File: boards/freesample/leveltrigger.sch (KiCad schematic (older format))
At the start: 0 parts

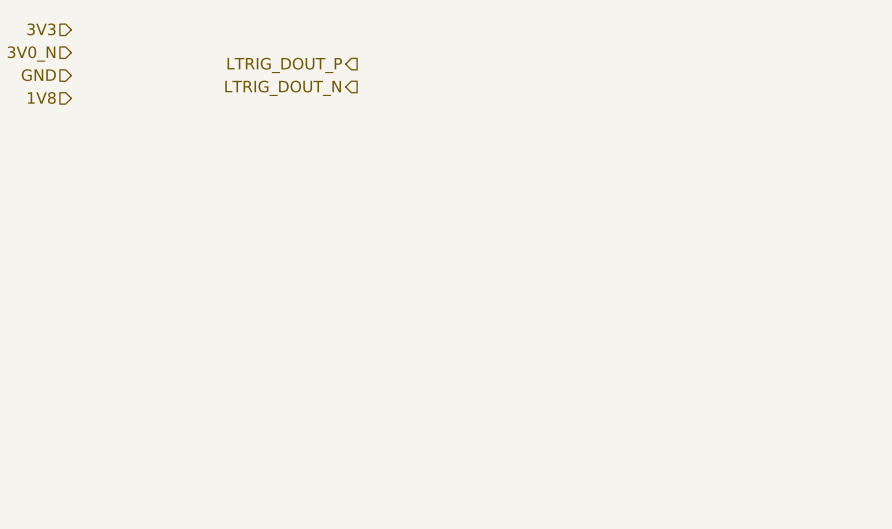
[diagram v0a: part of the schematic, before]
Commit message: Continued initial schematic capture
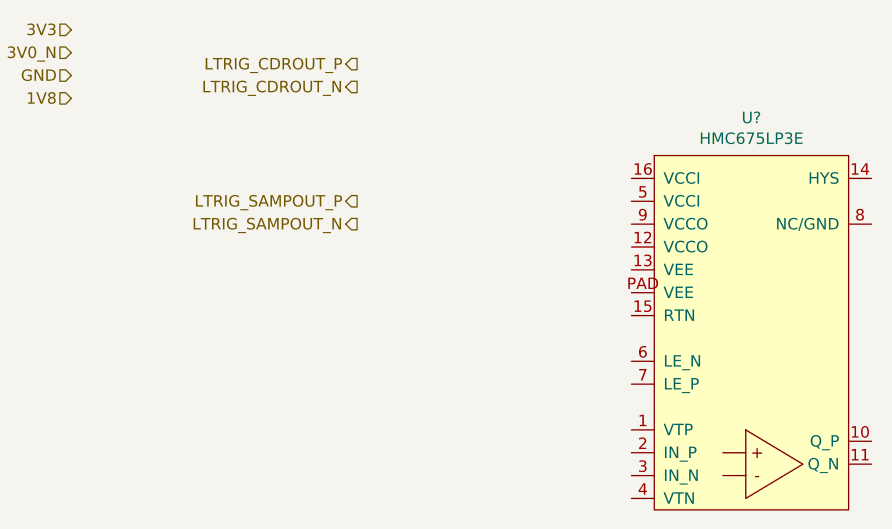
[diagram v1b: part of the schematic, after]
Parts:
- added U?: HMC675LP3E, symbol analog-azonenberg:HMC675LP3E
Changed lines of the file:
@@
 $Descr A4 11693 8268
 encoding utf-8
-Sheet 9 11
+Sheet 8 12
 Title "FREESAMPLE Oscilloscope"
-Date "2018-12-15"
+Date "2018-12-17"
 Rev "0.1"
 Comp "Andrew D. Zonenberg / Antikernel Labs"
@@
 LTRIG_DIN
 Text HLabel 5550 1650 0    50   Output ~ 0
-LTRIG_DOUT_P
+LTRIG_CDROUT_P
 Text HLabel 5550 1750 0    50   Output ~ 0
-LTRIG_DOUT_N
+LTRIG_CDROUT_N
 Text HLabel 4300 1500 0    50   Input ~ 0
 3V3
@@
 Text HLabel 3400 2100 0    50   Input ~ 0
 LTRIG_VT
+Text HLabel 5550 2250 0    50   Output ~ 0
+LTRIG_SAMPOUT_P
+Text HLabel 5550 2350 0    50   Output ~ 0
+LTRIG_SAMPOUT_N
+$Comp
+L analog-azonenberg:HMC675LP3E U?
+U 1 1 5C3D1034
+P 6850 3600
+F 0 "U?" H 7275 5315 50  0000 C CNN
+F 1 "HMC675LP3E" H 7275 5224 50  0000 C CNN
+F 2 "" H 6850 3600 50  0001 C CNN
+F 3 "" H 6850 3600 50  0001 C CNN
+	1    6850 3600
+	1    0    0    -1
+$EndComp
 $EndSCHEMATC

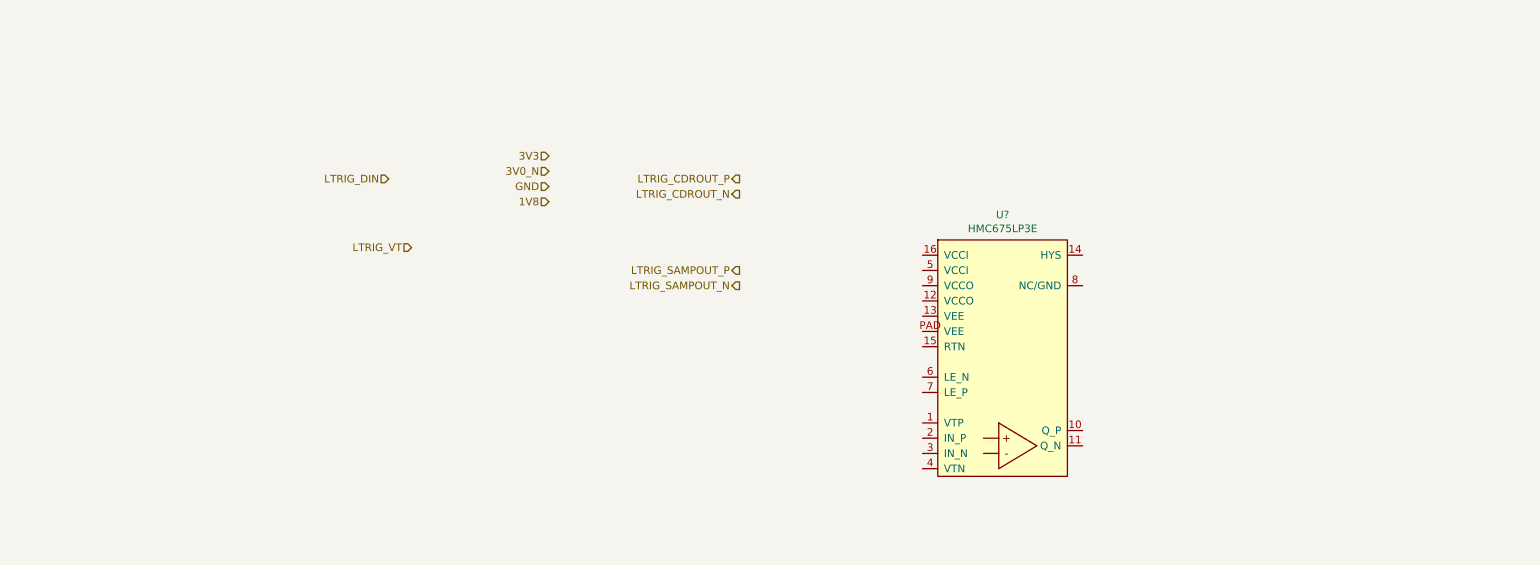
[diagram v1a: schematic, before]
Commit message: Continued initial schematic entry
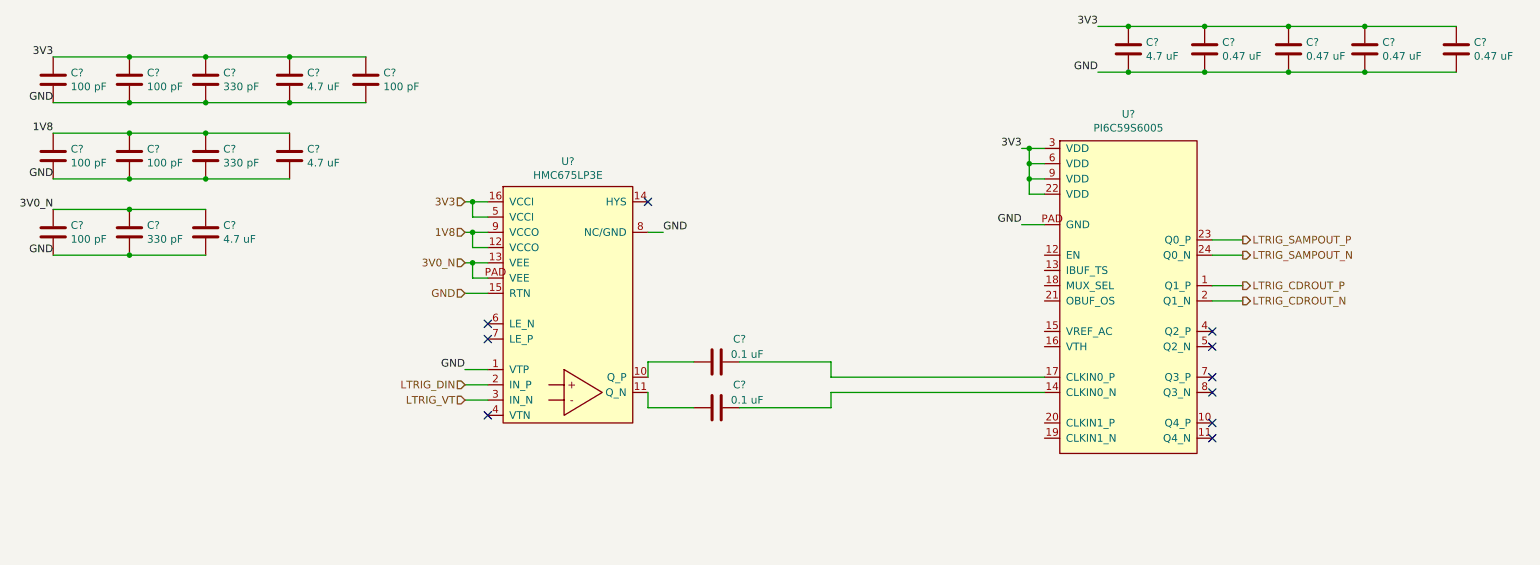
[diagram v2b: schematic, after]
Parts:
- added C? (x3): 330 pF, symbol device:C
- added C? (x6): 100 pF, symbol device:C
- added C? (x4): 4.7 uF, symbol device:C
- added C? (x4): 0.47 uF, symbol device:C
- added C? (x2): 0.1 uF, symbol device:C
- added U?: PI6C59S6005, symbol special-azonenberg:PI6C59S6005
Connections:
- net 1V8: now also U?.12 (VCCO), U?.9 (VCCO), C?.1, C?.1, C?.1, C?.1
- net 3V0_N: now also U?.13 (VEE), U?.PAD (VEE), C?.1, C?.1, C?.1
- net 3V3: now also U?.16 (VCCI), U?.5 (VCCI), C?.1, C?.1, C?.1, C?.1, C?.1, C?.1, C?.1, C?.1, C?.1, C?.1, U?.22 (VDD), U?.3 (VDD), U?.6 (VDD), U?.9 (VDD)
- net GND: now also U?.1 (VTP), U?.15 (RTN), U?.8 (NC/GND), C?.2, C?.2, C?.2, C?.2, C?.2, C?.2, C?.2, C?.2, C?.2, C?.2, C?.2, C?.2, C?.2, C?.2, C?.2, C?.2, C?.2, U?.PAD (GND)
- net LTRIG_CDROUT_N: now also U?.2 (Q1_N)
- net LTRIG_CDROUT_P: now also U?.1 (Q1_P)
- net LTRIG_DIN: now also U?.2 (IN_P)
- net LTRIG_SAMPOUT_N: now also U?.24 (Q0_N)
- net LTRIG_SAMPOUT_P: now also U?.23 (Q0_P)
- net LTRIG_VT: now also U?.3 (IN_N)
- net at U?.10 (Q_P): now also C?.2
- net at U?.11 (Q_N): now also C?.2
- new net: C?.1, U?.14 (CLKIN0_N)
- new net: C?.1, U?.17 (CLKIN0_P)
- no-connect marks 0 -> 10
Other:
- moved on the sheet: U?

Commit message: Continued work on schematic capture
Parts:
- gave numbers to parts that had none: 21
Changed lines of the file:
@@
 LTRIG_SAMPOUT_N
 $Comp
-L analog-azonenberg:HMC675LP3E U?
+L analog-azonenberg:HMC675LP3E U9
 U 1 1 5C3D1034
 P 4000 3250
-F 0 "U?" H 4425 4965 50  0000 C CNN
+F 0 "U9" H 4425 4965 50  0000 C CNN
 F 1 "HMC675LP3E" H 4425 4874 50  0000 C CNN
 F 2 "" H 4000 3250 50  0001 C CNN
@@
 P 2050 1000
 AR Path="/5C0E404A/5C5773C7" Ref="C?"  Part="1"
-AR Path="/5C23AE1C/5C5773C7" Ref="C?"  Part="1"
-F 0 "C?" H 2165 1046 50  0000 L CNN
+AR Path="/5C23AE1C/5C5773C7" Ref="C43"  Part="1"
+F 0 "C43" H 2165 1046 50  0000 L CNN
 F 1 "330 pF" H 2165 955 50  0000 L CNN
 F 2 "" H 2088 850 50  0001 C CNN
@@
 P 1550 1000
 AR Path="/5C0E404A/5C5773CD" Ref="C?"  Part="1"
-AR Path="/5C23AE1C/5C5773CD" Ref="C?"  Part="1"
-F 0 "C?" H 1665 1046 50  0000 L CNN
+AR Path="/5C23AE1C/5C5773CD" Ref="C40"  Part="1"
+F 0 "C40" H 1665 1046 50  0000 L CNN
 F 1 "100 pF" H 1665 955 50  0000 L CNN
 F 2 "" H 1588 850 50  0001 C CNN
@@
 P 1050 1000
 AR Path="/5C0E404A/5C5773D3" Ref="C?"  Part="1"
-AR Path="/5C23AE1C/5C5773D3" Ref="C?"  Part="1"
-F 0 "C?" H 1165 1046 50  0000 L CNN
+AR Path="/5C23AE1C/5C5773D3" Ref="C37"  Part="1"
+F 0 "C37" H 1165 1046 50  0000 L CNN
 F 1 "100 pF" H 1165 955 50  0000 L CNN
 F 2 "" H 1088 850 50  0001 C CNN
@@
 P 2600 1000
 AR Path="/5C0E404A/5C5773DB" Ref="C?"  Part="1"
-AR Path="/5C23AE1C/5C5773DB" Ref="C?"  Part="1"
-F 0 "C?" H 2715 1046 50  0000 L CNN
+AR Path="/5C23AE1C/5C5773DB" Ref="C46"  Part="1"
+F 0 "C46" H 2715 1046 50  0000 L CNN
 F 1 "4.7 uF" H 2715 955 50  0000 L CNN
 F 2 "" H 2638 850 50  0001 C CNN
@@
 P 3100 1000
 AR Path="/5C0E404A/5C5773EB" Ref="C?"  Part="1"
-AR Path="/5C23AE1C/5C5773EB" Ref="C?"  Part="1"
-F 0 "C?" H 3215 1046 50  0000 L CNN
+AR Path="/5C23AE1C/5C5773EB" Ref="C48"  Part="1"
+F 0 "C48" H 3215 1046 50  0000 L CNN
 F 1 "100 pF" H 3215 955 50  0000 L CNN
 F 2 "" H 3138 850 50  0001 C CNN
@@
 P 2050 1500
 AR Path="/5C0E404A/5C5773F5" Ref="C?"  Part="1"
-AR Path="/5C23AE1C/5C5773F5" Ref="C?"  Part="1"
-F 0 "C?" H 2165 1546 50  0000 L CNN
+AR Path="/5C23AE1C/5C5773F5" Ref="C44"  Part="1"
+F 0 "C44" H 2165 1546 50  0000 L CNN
 F 1 "330 pF" H 2165 1455 50  0000 L CNN
 F 2 "" H 2088 1350 50  0001 C CNN
@@
 P 1550 1500
 AR Path="/5C0E404A/5C5773FB" Ref="C?"  Part="1"
-AR Path="/5C23AE1C/5C5773FB" Ref="C?"  Part="1"
-F 0 "C?" H 1665 1546 50  0000 L CNN
+AR Path="/5C23AE1C/5C5773FB" Ref="C41"  Part="1"
+F 0 "C41" H 1665 1546 50  0000 L CNN
 F 1 "100 pF" H 1665 1455 50  0000 L CNN
 F 2 "" H 1588 1350 50  0001 C CNN
@@
 P 1050 1500
 AR Path="/5C0E404A/5C577401" Ref="C?"  Part="1"
-AR Path="/5C23AE1C/5C577401" Ref="C?"  Part="1"
-F 0 "C?" H 1165 1546 50  0000 L CNN
+AR Path="/5C23AE1C/5C577401" Ref="C38"  Part="1"
+F 0 "C38" H 1165 1546 50  0000 L CNN
 F 1 "100 pF" H 1165 1455 50  0000 L CNN
 F 2 "" H 1088 1350 50  0001 C CNN
@@
 P 2600 1500
 AR Path="/5C0E404A/5C577409" Ref="C?"  Part="1"
-AR Path="/5C23AE1C/5C577409" Ref="C?"  Part="1"
-F 0 "C?" H 2715 1546 50  0000 L CNN
+AR Path="/5C23AE1C/5C577409" Ref="C47"  Part="1"
+F 0 "C47" H 2715 1546 50  0000 L CNN
 F 1 "4.7 uF" H 2715 1455 50  0000 L CNN
 F 2 "" H 2638 1350 50  0001 C CNN
@@
 P 1050 2000
 AR Path="/5C0E404A/5C57741A" Ref="C?"  Part="1"
-AR Path="/5C23AE1C/5C57741A" Ref="C?"  Part="1"
-F 0 "C?" H 1165 2046 50  0000 L CNN
+AR Path="/5C23AE1C/5C57741A" Ref="C39"  Part="1"
+F 0 "C39" H 1165 2046 50  0000 L CNN
 F 1 "100 pF" H 1165 1955 50  0000 L CNN
 F 2 "" H 1088 1850 50  0001 C CNN
@@
 P 1550 2000
 AR Path="/5C0E404A/5C577420" Ref="C?"  Part="1"
-AR Path="/5C23AE1C/5C577420" Ref="C?"  Part="1"
-F 0 "C?" H 1665 2046 50  0000 L CNN
+AR Path="/5C23AE1C/5C577420" Ref="C42"  Part="1"
+F 0 "C42" H 1665 2046 50  0000 L CNN
 F 1 "330 pF" H 1665 1955 50  0000 L CNN
 F 2 "" H 1588 1850 50  0001 C CNN
@@
 P 2050 2000
 AR Path="/5C0E404A/5C577426" Ref="C?"  Part="1"
-AR Path="/5C23AE1C/5C577426" Ref="C?"  Part="1"
-F 0 "C?" H 2165 2046 50  0000 L CNN
+AR Path="/5C23AE1C/5C577426" Ref="C45"  Part="1"
+F 0 "C45" H 2165 2046 50  0000 L CNN
 F 1 "4.7 uF" H 2165 1955 50  0000 L CNN
 F 2 "" H 2088 1850 50  0001 C CNN
@@
 P 7650 3450
 AR Path="/5C0E404A/5C5902BE" Ref="U?"  Part="1"
-AR Path="/5C23AE1C/5C5902BE" Ref="U?"  Part="1"
-F 0 "U?" H 8100 5675 50  0000 C CNN
+AR Path="/5C23AE1C/5C5902BE" Ref="U10"  Part="1"
+F 0 "U10" H 8100 5675 50  0000 C CNN
 F 1 "PI6C59S6005" H 8100 5584 50  0000 C CNN
 F 2 "" H 7650 3150 50  0001 C CNN
@@
 $EndComp
 $Comp
-L device:C C?
+L device:C C51
 U 1 1 5C5902C4
 P 8100 800
-F 0 "C?" H 8215 846 50  0000 L CNN
+F 0 "C51" H 8215 846 50  0000 L CNN
 F 1 "4.7 uF" H 8215 755 50  0000 L CNN
 F 2 "" H 8138 650 50  0001 C CNN
@@
 $EndComp
 $Comp
-L device:C C?
+L device:C C52
 U 1 1 5C5902CA
 P 8600 800
-F 0 "C?" H 8715 846 50  0000 L CNN
+F 0 "C52" H 8715 846 50  0000 L CNN
 F 1 "0.47 uF" H 8715 755 50  0000 L CNN
 F 2 "" H 8638 650 50  0001 C CNN
@@
 $EndComp
 $Comp
-L device:C C?
+L device:C C54
 U 1 1 5C5902D0
 P 9650 800
-F 0 "C?" H 9765 846 50  0000 L CNN
+F 0 "C54" H 9765 846 50  0000 L CNN
 F 1 "0.47 uF" H 9765 755 50  0000 L CNN
 F 2 "" H 9688 650 50  0001 C CNN
@@
 	8600 950  9150 950
 $Comp
-L device:C C?
+L device:C C53
 U 1 1 5C5902E2
 P 9150 800
-F 0 "C?" H 9265 846 50  0000 L CNN
+F 0 "C53" H 9265 846 50  0000 L CNN
 F 1 "0.47 uF" H 9265 755 50  0000 L CNN
 F 2 "" H 9188 650 50  0001 C CNN
@@
 	9150 950  9650 950
 $Comp
-L device:C C?
+L device:C C55
 U 1 1 5C5902EC
 P 10250 800
-F 0 "C?" H 10365 846 50  0000 L CNN
+F 0 "C55" H 10365 846 50  0000 L CNN
 F 1 "0.47 uF" H 10365 755 50  0000 L CNN
 F 2 "" H 10288 650 50  0001 C CNN
@@
 NoConn ~ 3900 2700
 $Comp
-L device:C C?
+L device:C C49
 U 1 1 5C59BBB6
 P 5400 2850
-F 0 "C?" V 5250 3000 50  0000 C CNN
+F 0 "C49" V 5250 3000 50  0000 C CNN
 F 1 "0.1 uF" V 5350 3050 50  0000 C CNN
 F 2 "" H 5438 2700 50  0001 C CNN
@@
 $EndComp
 $Comp
-L device:C C?
+L device:C C50
 U 1 1 5C59C861
 P 5400 3150
-F 0 "C?" V 5250 3300 50  0000 C CNN
+F 0 "C50" V 5250 3300 50  0000 C CNN
 F 1 "0.1 uF" V 5350 3350 50  0000 C CNN
 F 2 "" H 5438 3000 50  0001 C CNN

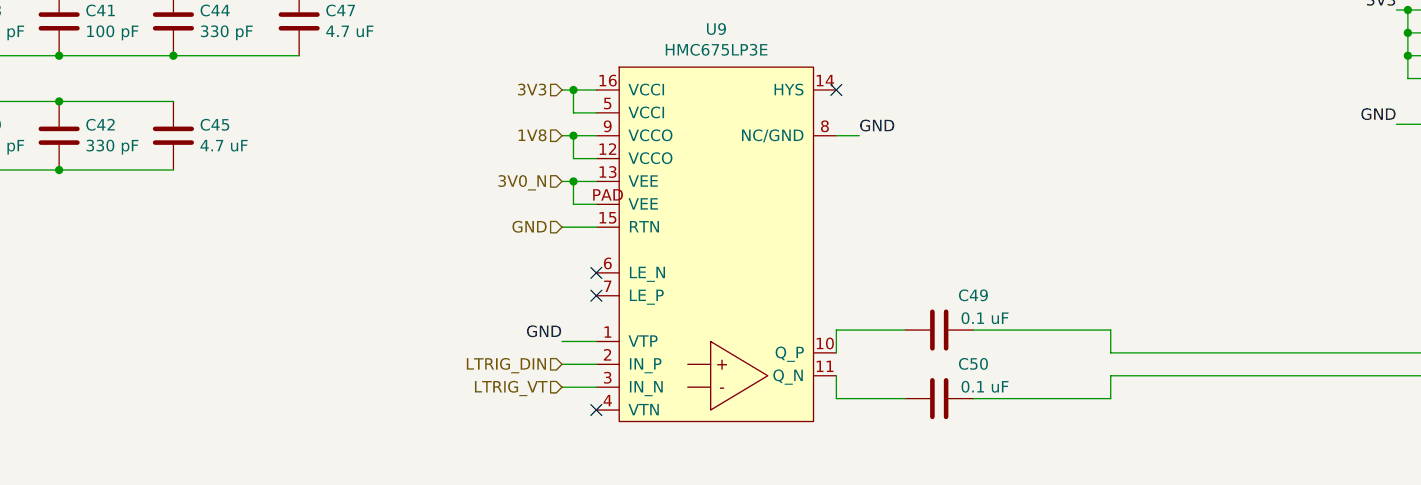
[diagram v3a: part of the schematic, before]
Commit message: Continued work on FREESAMPLE schematic including PSU.
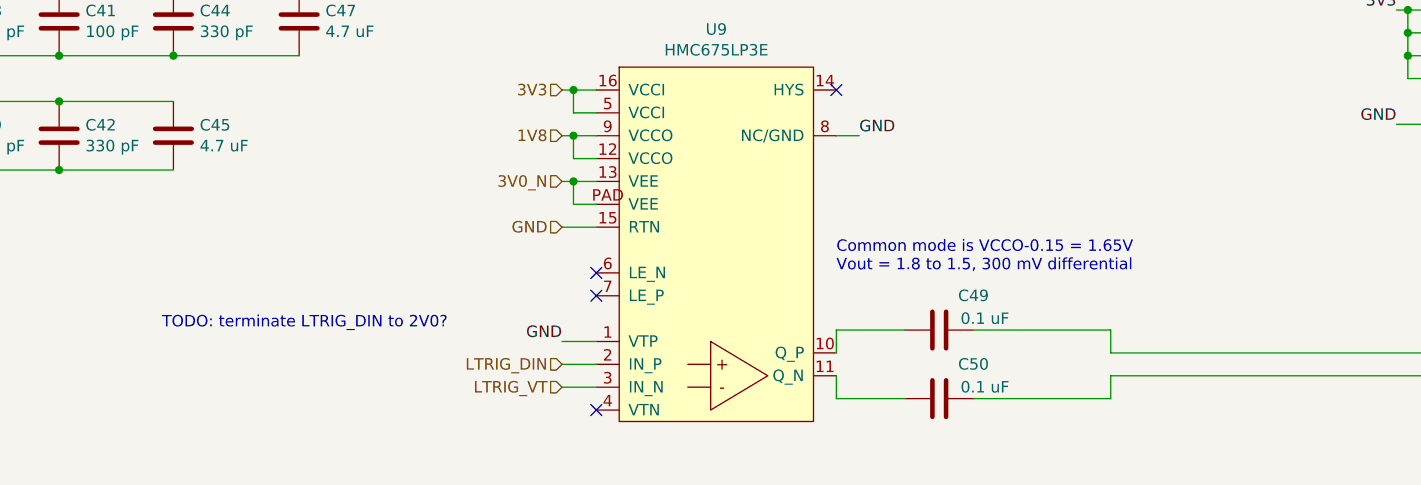
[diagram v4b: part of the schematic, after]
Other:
- note added: "Common mode is VCCO-0.15 = 1.65V\nVout = 1.8 to 1.5, 300 mV differential"
- note added: "TODO: terminate LTRIG_DIN to 2V0?"
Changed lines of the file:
@@
 Sheet 8 12
 Title "FREESAMPLE Oscilloscope"
-Date "2018-12-17"
+Date "2019-02-23"
 Rev "0.1"
 Comp "Andrew D. Zonenberg / Antikernel Labs"
@@
 Wire Wire Line
 	8650 2450 8850 2450
+Text Notes 2000 2850 0    50   ~ 0
+TODO: terminate LTRIG_DIN to 2V0?
+Text Notes 4950 2600 0    50   ~ 0
+Common mode is VCCO-0.15 = 1.65V\nVout = 1.8 to 1.5, 300 mV differential
 $EndSCHEMATC

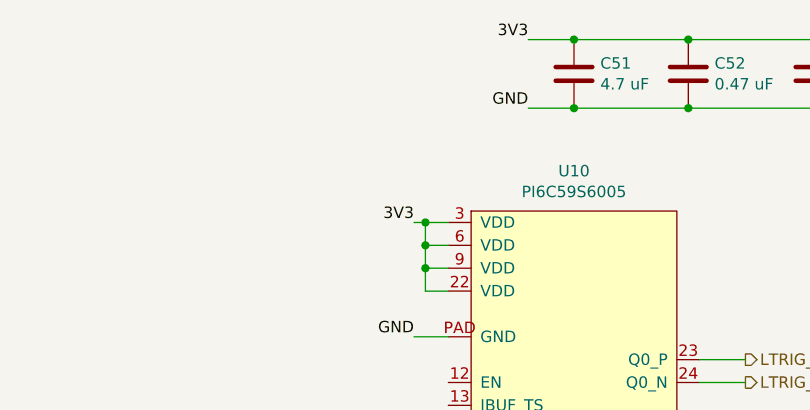
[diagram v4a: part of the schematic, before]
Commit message: Hooked up new power rails
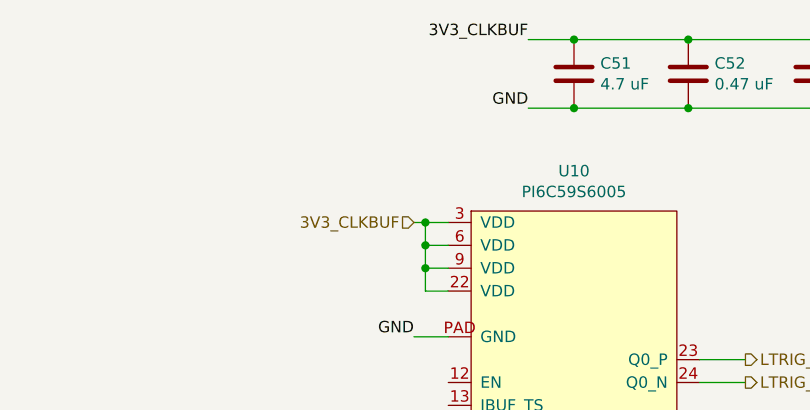
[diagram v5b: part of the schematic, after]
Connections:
- net 3V3: no longer C51.1, C52.1, C53.1, C54.1, C55.1, U10.22 (VDD), U10.3 (VDD), U10.6 (VDD), U10.9 (VDD)
- new net 3V3_CLKBUF: C51.1, C52.1, C53.1, C54.1, C55.1, U10.22 (VDD), U10.3 (VDD), U10.6 (VDD), U10.9 (VDD)
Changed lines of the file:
@@
 Sheet 8 12
 Title "FREESAMPLE Oscilloscope"
-Date "2019-02-23"
+Date "2019-02-26"
 Rev "0.1"
 Comp "Andrew D. Zonenberg / Antikernel Labs"
@@
 	8600 950  8100 950
 Text Label 7900 650  2    50   ~ 0
-3V3
+3V3_CLKBUF
 Wire Wire Line
 	7900 650  8100 650
@@
 Wire Wire Line
 	6150 2950 7550 2950
-Text Label 7400 1450 2    50   ~ 0
-3V3
 Wire Wire Line
 	7400 1450 7450 1450
@@
 Text Notes 4950 2600 0    50   ~ 0
 Common mode is VCCO-0.15 = 1.65V\nVout = 1.8 to 1.5, 300 mV differential
+Text HLabel 7400 1450 0    50   Input ~ 0
+3V3_CLKBUF
 $EndSCHEMATC
